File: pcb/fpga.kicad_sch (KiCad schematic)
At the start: 23 parts, among them J13 KB, U2 XC2S100TQ144, Y1 TXC-7C, Y2 GTXO-14T

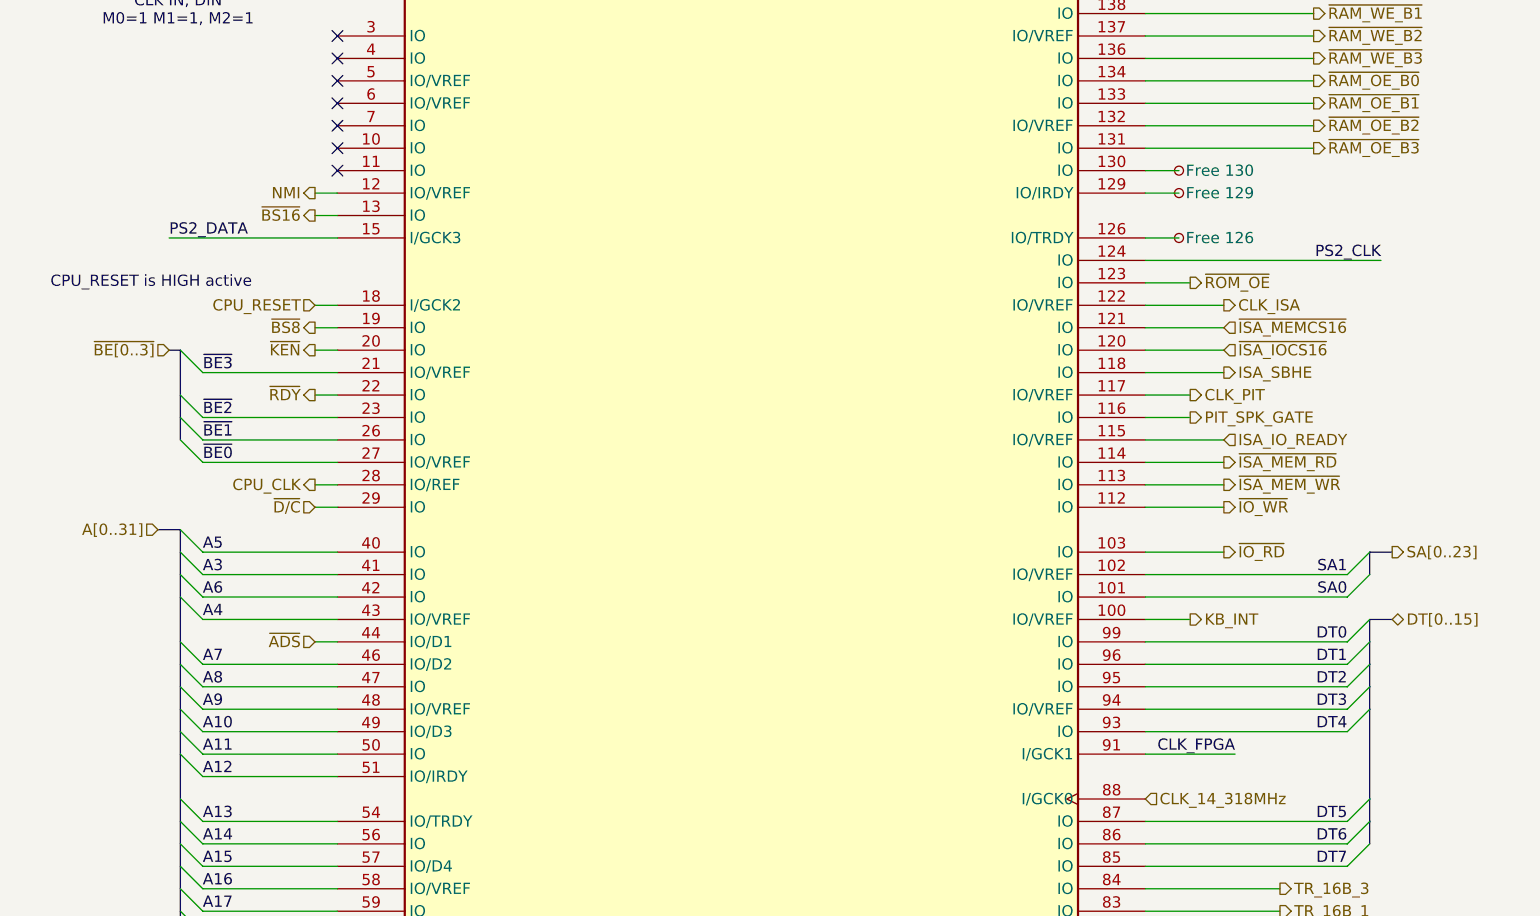
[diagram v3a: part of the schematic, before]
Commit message: cant use I/GCK for generic input after all, moving ps2_data to another IO. CLKDV_DIVIDE => 12.0 uses two DLLs and blocks CLK_IN_14_318 from using GCK0 -> moving CLK_FPGA to GCK3 instead.
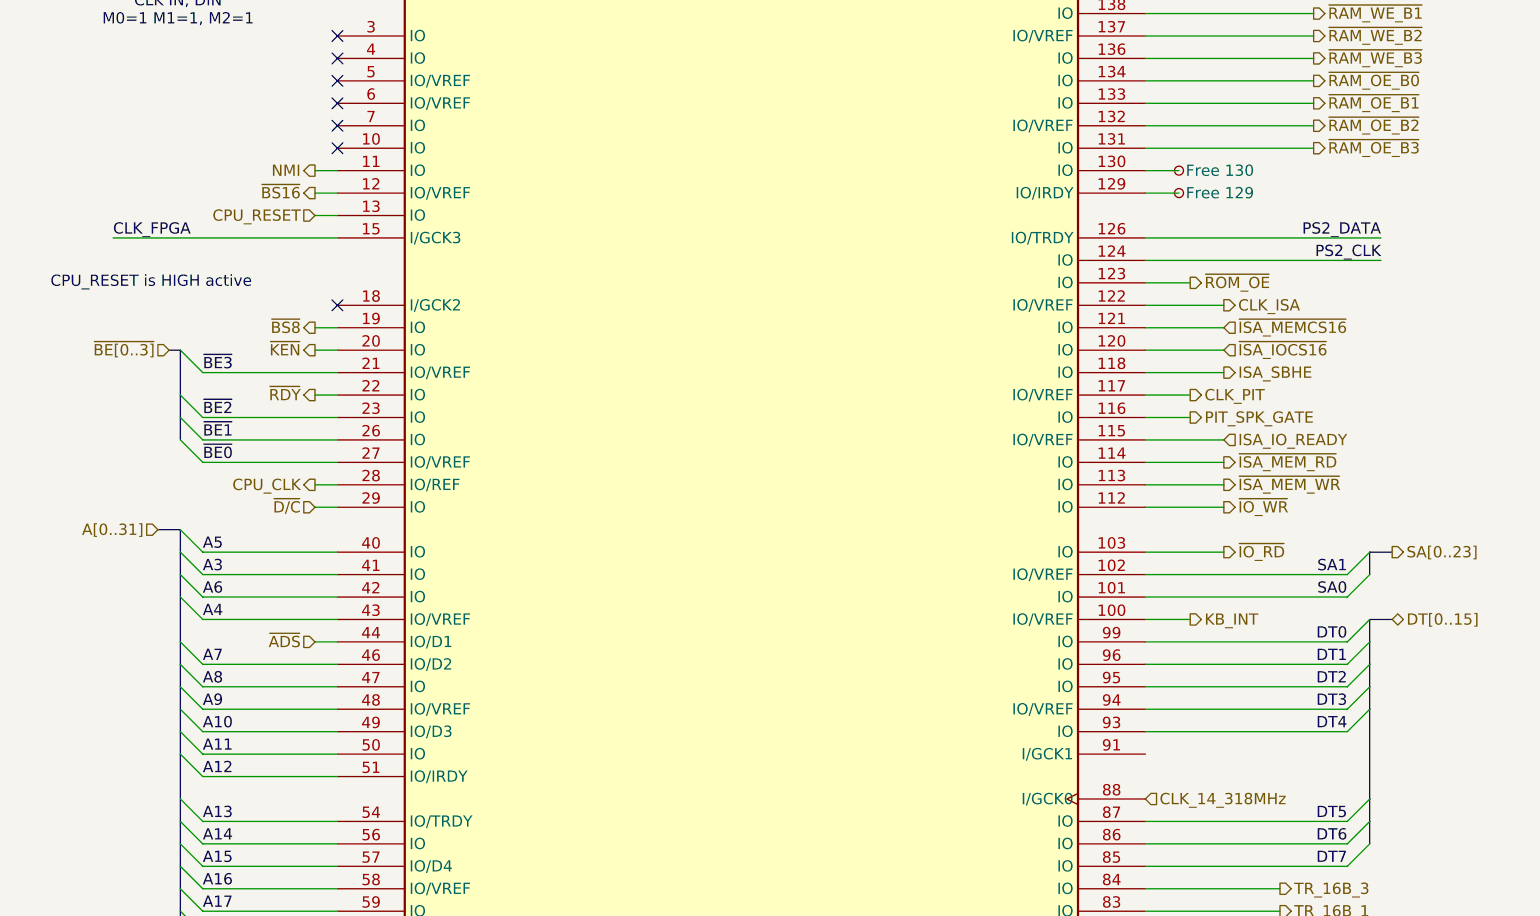
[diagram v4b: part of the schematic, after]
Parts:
- removed TP15: Free 126, 486custom:TestPoint_Pad_D0.4mm, symbol Connector:TestPoint_Small
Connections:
- net CLK_FPGA: now also U2.15 (I/GCK3); no longer U2.91 (I/GCK1)
- net CPU_RESET: now also U2.13 (IO); no longer U2.18 (I/GCK2)
- net NMI: now also U2.11 (IO); no longer U2.12 (IO/VREF)
- net PS2_DATA: now also U2.126 (IO/TRDY); no longer U2.15 (I/GCK3)
- net ~{BS16}: now also U2.12 (IO/VREF); no longer U2.13 (IO)
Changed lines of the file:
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@@
 	)
 	(no_connect
+		(at 48.26 96.52)
+	)
+	(no_connect
 		(at 48.26 71.12)
 	)
@@
 	)
 	(no_connect
-		(at 48.26 81.28)
-	)
-	(no_connect
 		(at 200.66 83.82)
 	)
@@
 	(wire
 		(pts
+			(xy 45.72 81.28) (xy 48.26 81.28)
+		)
+		(stroke
+			(width 0)
+			(type default)
+		)
+	)
+	(wire
+		(pts
 			(xy 33.02 144.78) (xy 48.26 144.78)
 		)
@@
 	(wire
 		(pts
+			(xy 139.7 88.9) (xy 166.37 88.9)
+		)
+		(stroke
+			(width 0)
+			(type default)
+		)
+	)
+	(wire
+		(pts
 			(xy 44.45 33.02) (xy 48.26 33.02)
 		)
@@
 		)
 	)
-	(wire
-		(pts
-			(xy 45.72 83.82) (xy 48.26 83.82)
-		)
-		(stroke
-			(width 0)
-			(type default)
-		)
-	)
 	(bus
 		(pts
@@
 	(wire
 		(pts
-			(xy 139.7 147.32) (xy 149.86 147.32)
-		)
-		(stroke
-			(width 0)
-			(type default)
-		)
-	)
-	(wire
-		(pts
 			(xy 33.02 104.14) (xy 48.26 104.14)
 		)
@@
 	(wire
 		(pts
-			(xy 48.26 88.9) (xy 29.21 88.9)
-		)
-		(stroke
-			(width 0)
-			(type default)
-		)
-	)
-	(wire
-		(pts
 			(xy 271.78 153.67) (xy 271.78 154.94)
 		)
@@
 	(wire
 		(pts
-			(xy 139.7 88.9) (xy 143.51 88.9)
-		)
-		(stroke
-			(width 0)
-			(type default)
-		)
-	)
-	(wire
-		(pts
 			(xy 139.7 165.1) (xy 154.94 165.1)
 		)
@@
 		)
 	)
+	(wire
+		(pts
+			(xy 48.26 88.9) (xy 22.86 88.9)
+		)
+		(stroke
+			(width 0)
+			(type default)
+		)
+	)
 	(bus
 		(pts
@@
 	(wire
 		(pts
+			(xy 45.72 83.82) (xy 48.26 83.82)
+		)
+		(stroke
+			(width 0)
+			(type default)
+		)
+	)
+	(wire
+		(pts
 			(xy 45.72 48.26) (xy 48.26 48.26)
 		)
@@
 	(wire
 		(pts
+			(xy 45.72 86.36) (xy 48.26 86.36)
+		)
+		(stroke
+			(width 0)
+			(type default)
+		)
+	)
+	(wire
+		(pts
 			(xy 99.06 19.05) (xy 101.6 19.05)
 		)
@@
 	(wire
 		(pts
-			(xy 45.72 96.52) (xy 48.26 96.52)
-		)
-		(stroke
-			(width 0)
-			(type default)
-		)
-	)
-	(wire
-		(pts
 			(xy 203.2 154.94) (xy 193.04 154.94)
 		)
@@
 	(wire
 		(pts
-			(xy 45.72 86.36) (xy 48.26 86.36)
-		)
-		(stroke
-			(width 0)
-			(type default)
-		)
-	)
-	(wire
-		(pts
 			(xy 208.28 154.94) (xy 203.2 154.94)
 		)
@@
 		)
 	)
+	(label "PS2_DATA"
+		(at 166.37 88.9 180)
+		(effects
+			(font
+				(size 1.27 1.27)
+			)
+			(justify right bottom)
+		)
+	)
 	(label "PS2_CLK"
 		(at 166.37 91.44 180)
@@
 		)
 	)
-	(label "PS2_DATA"
-		(at 29.21 88.9 0)
-		(effects
-			(font
-				(size 1.27 1.27)
-			)
-			(justify left bottom)
-		)
-	)
 	(label "A13"
 		(at 33.02 154.94 0)
@@
 		)
 	)
+	(label "CLK_FPGA"
+		(at 22.86 88.9 0)
+		(effects
+			(font
+				(size 1.27 1.27)
+			)
+			(justify left bottom)
+		)
+	)
 	(label "A6"
 		(at 33.02 129.54 0)
@@
 		)
 	)
-	(label "CLK_FPGA"
-		(at 149.86 147.32 180)
-		(effects
-			(font
-				(size 1.27 1.27)
-			)
-			(justify right bottom)
-		)
-	)
 	(label "A7"
 		(at 33.02 137.16 0)
@@
 		)
 	)
-	(hierarchical_label "~{BS16}"
-		(shape output)
-		(at 45.72 86.36 180)
-		(effects
-			(font
-				(size 1.27 1.27)
-			)
-			(justify right)
-		)
-	)
 	(hierarchical_label "ISA_SBHE"
 		(shape output)
@@
 		)
 	)
+	(hierarchical_label "NMI"
+		(shape output)
+		(at 45.72 81.28 180)
+		(effects
+			(font
+				(size 1.27 1.27)
+			)
+			(justify right)
+		)
+	)
 	(hierarchical_label "~{PIC_CS}"
 		(shape output)
@@
 		)
 	)
-	(hierarchical_label "CPU_RESET"
-		(shape input)
-		(at 45.72 96.52 180)
-		(effects
-			(font
-				(size 1.27 1.27)
-			)
-			(justify right)
-		)
-	)
 	(hierarchical_label "~{RAM_WE_B1}"
 		(shape output)
@@
 		)
 	)
-	(hierarchical_label "NMI"
-		(shape output)
-		(at 45.72 83.82 180)
-		(effects
-			(font
-				(size 1.27 1.27)
-			)
-			(justify right)
-		)
-	)
 	(hierarchical_label "TR_16B_1"
 		(shape output)
@@
 		)
 	)
+	(hierarchical_label "~{BS16}"
+		(shape output)
+		(at 45.72 83.82 180)
+		(effects
+			(font
+				(size 1.27 1.27)
+			)
+			(justify right)
+		)
+	)
 	(hierarchical_label "KB_INT"
 		(shape output)
@@
 		)
 	)
+	(hierarchical_label "CPU_RESET"
+		(shape input)
+		(at 45.72 86.36 180)
+		(effects
+			(font
+				(size 1.27 1.27)
+			)
+			(justify right)
+		)
+	)
 	(symbol
 		(lib_id "Device:C")
@@
 					(unit 1)
 				)
-			)
-		)
-	)
-	(symbol
-		(lib_id "Connector:TestPoint_Small")
-		(at 143.51 88.9 0)
-		(unit 1)
-		(exclude_from_sim no)
-		(in_bom yes)
-		(on_board yes)
-		(dnp no)
-		(property "Reference" "TP15"
-			(at 137.16 88.9 0)
-			(effects
-				(font
-					(size 1.27 1.27)
-				)
-				(justify left)
-				(hide yes)
-			)
-		)
-		(property "Value" "Free 126"
-			(at 144.272 88.9 0)
-			(effects
-				(font
-					(size 1.27 1.27)
-				)
-				(justify left)
-			)
-		)
-		(property "Footprint" "486custom:TestPoint_Pad_D0.4mm"
-			(at 148.59 88.9 0)
-			(effects
-				(font
-					(size 1.27 1.27)
-				)
-				(hide yes)
-			)
-		)
-		(property "Datasheet" "~"
-			(at 148.59 88.9 0)
-			(effects
-				(font
-					(size 1.27 1.27)
-				)
-				(hide yes)
-			)
-		)
-		(property "Description" "test point"
-			(at 143.51 88.9 0)
-			(effects
-				(font
-					(size 1.27 1.27)
-				)
-				(hide yes)
-			)
-		)
-		(pin "1"
-		)
-		(instances
-			(project "homebrew_486"
-				(path "/360fb3b9-a21a-4226-8954-bf45cf17bb35/49c3128c-49f0-451c-bde3-bf7412e8a8c9"
-					(reference "TP15")
-					(unit 1)
-				)

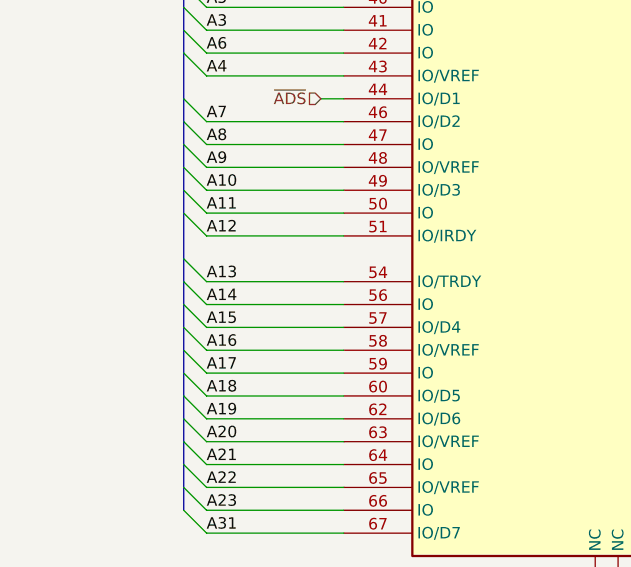
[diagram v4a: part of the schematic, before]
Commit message: PCB flip GND and power layers around, FPGA remap A12 for better routing
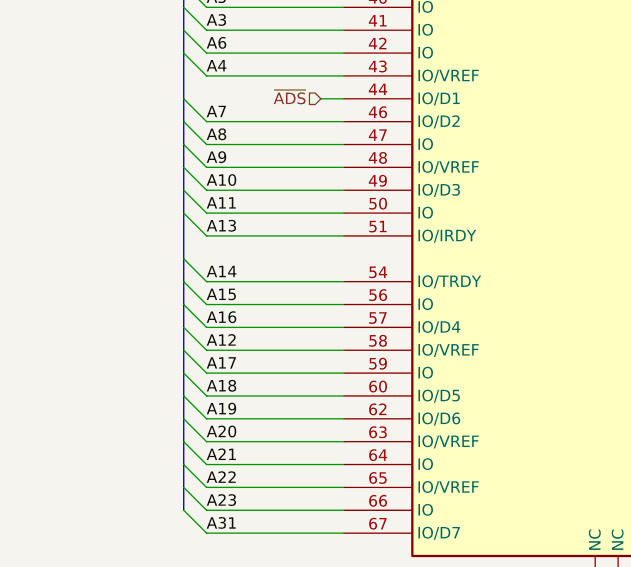
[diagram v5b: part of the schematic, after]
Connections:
- net A12: now also U2.58 (IO/VREF); no longer U2.51 (IO/IRDY)
- net A13: now also U2.51 (IO/IRDY); no longer U2.54 (IO/TRDY)
- net A14: now also U2.54 (IO/TRDY); no longer U2.56 (IO)
- net A15: now also U2.56 (IO); no longer U2.57 (IO/D4)
- net A16: now also U2.57 (IO/D4); no longer U2.58 (IO/VREF)
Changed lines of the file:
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@@
+		)
+	)
+	(label "A15"
+		(at 33.02 157.48 0)
+		(effects
+			(font
+				(size 1.27 1.27)
+			)
+			(justify left bottom)
 		)
 	)
@@
 		)
 	)
+	(label "A14"
+		(at 33.02 154.94 0)
+		(effects
+			(font
+				(size 1.27 1.27)
+			)
+			(justify left bottom)
+		)
+	)
 	(label "SA0"
 		(at 162.56 129.54 180)
@@
 		)
 	)
+	(label "A13"
+		(at 33.02 149.86 0)
+		(effects
+			(font
+				(size 1.27 1.27)
+			)
+			(justify left bottom)
+		)
+	)
 	(label "A8"
 		(at 33.02 139.7 0)
@@
 		)
 	)
-	(label "A13"
-		(at 33.02 154.94 0)
-		(effects
-			(font
-				(size 1.27 1.27)
-			)
-			(justify left bottom)
-		)
-	)
 	(label "A18"
 		(at 33.02 167.64 0)
@@
 		)
 	)
-	(label "A14"
-		(at 33.02 157.48 0)
-		(effects
-			(font
-				(size 1.27 1.27)
-			)
-			(justify left bottom)
-		)
-	)
 	(label "A19"
 		(at 33.02 170.18 0)
@@
 		)
 	)
-	(label "A12"
-		(at 33.02 149.86 0)
+	(label "A16"
+		(at 33.02 160.02 0)
 		(effects
 			(font
@@
 		)
 	)
+	(label "A12"
+		(at 33.02 162.56 0)
+		(effects
+			(font
+				(size 1.27 1.27)
+			)
+			(justify left bottom)
+		)
+	)
 	(label "A5"
 		(at 33.02 124.46 0)
@@
 		)
 	)
-	(label "A15"
-		(at 33.02 160.02 0)
-		(effects
-			(font
-				(size 1.27 1.27)
-			)
-			(justify left bottom)
-		)
-	)
 	(label "DT7"
 		(at 162.56 160.02 180)
@@
 		)
 	)
-	(label "A16"
-		(at 33.02 162.56 0)
-		(effects
-			(font
-				(size 1.27 1.27)
-			)
-			(justify left bottom)
-		)
-	)
